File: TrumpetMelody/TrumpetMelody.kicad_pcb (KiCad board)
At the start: 2 copper layers, 76.2 x 68.6 mm, 81 parts, among them J1 USB_B_Micro, J2 Conn_01x05, J3 640456-3, J4 640456-3, SW1 SW_Push, U1 STM32F411RETx, U2 TLV62565DBVR, U3 MAX98357AETE_T, U4 MAX7375AXR805

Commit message: added alligator
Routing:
- net GND: vias 145 -> 146
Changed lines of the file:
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@@
   (via (at 165.735 83.058) (size 0.6604) (drill 0.381) (layers "F.Cu" "B.Cu") (free) (net 2))
   (via (at 203.105 102.37) (size 0.6604) (drill 0.381) (layers "F.Cu" "B.Cu") (free) (net 2))
+  (via (at 220.853 90.678) (size 1.8) (drill 0.9) (layers "F.Cu" "B.Cu") (net 2))
   (via (at 203.605 105.37) (size 0.6604) (drill 0.381) (layers "F.Cu" "B.Cu") (free) (net 2))
   (via (at 199.105 111.87) (size 0.6604) (drill 0.381) (layers "F.Cu" "B.Cu") (free) (net 2))

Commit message: cleaning
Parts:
- moved R25 1.53 mm to (197.6, 91.6)
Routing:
- net NJTRST: track 12.5 -> 13.6 mm
- net Net-(J2-Pin_5): track 2.96 -> 3.81 mm
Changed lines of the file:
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@@
   )
   (footprint "Resistor_SMD:R_0805_2012Metric_Pad1.20x1.40mm_HandSolder" (layer "F.Cu")
-    (at 196.287107 90.877107 -45)
+    (at 197.636622 91.606177 -45)
     (descr "Resistor SMD 0805 (2012 Metric), square (rectangular) end terminal, IPC_7351 nominal with elongated pad for handsoldering. (Body size source: IPC-SM-782 page 72, https://www.pcb-3d.com/wordpress/wp-content/uploads/ipc-sm-782a_amendment_1_and_2.pdf), generated with kicad-footprint-generator")
     (tags "resistor handsolder")
@@
   (segment (start 191.355 74.37) (end 191.355 75.681253) (width 0.254) (layer "B.Cu") (net 4))
   (segment (start 178.20837 66.87) (end 192.647803 66.87) (width 0.5) (layer "B.Cu") (net 4))
-  (segment (start 172.041482 67.375745) (end 172.054488 67.362739) (width 0.254) (layer "B.Cu") (net 4))
   (segment (start 170.545712 67.375745) (end 169.057454 67.375745) (width 0.5) (layer "B.Cu") (net 4))
   (segment (start 190.811123 79.038) (end 190.473126 79.038) (width 0.254) (layer "F.Cu") (net 5))
@@
   (via (at 205.105 88.62) (size 0.6604) (drill 0.381) (layers "F.Cu" "B.Cu") (free) (net 11))
   (segment (start 211.857768 68.152648) (end 211.857768 72.392265) (width 0.254) (layer "B.Cu") (net 11))
-  (segment (start 205.105 88.62) (end 195.605 88.62) (width 0.254) (layer "B.Cu") (net 11))
   (segment (start 211.84006 68.13494) (end 211.857768 68.152648) (width 0.254) (layer "B.Cu") (net 11))
-  (segment (start 192.903586 91.321414) (end 188.653585 91.321414) (width 0.254) (layer "B.Cu") (net 11))
-  (segment (start 195.605 88.62) (end 192.903586 91.321414) (width 0.254) (layer "B.Cu") (net 11))
+  (segment (start 196.6877 88.62) (end 193.986286 91.321414) (width 0.254) (layer "B.Cu") (net 11))
+  (segment (start 205.105 88.62) (end 196.6877 88.62) (width 0.254) (layer "B.Cu") (net 11))
+  (segment (start 193.986286 91.321414) (end 188.653585 91.321414) (width 0.254) (layer "B.Cu") (net 11))
   (segment (start 204.273075 58.783961) (end 203.233946 59.82309) (width 0.254) (layer "F.Cu") (net 12))
   (segment (start 203.168 55.9054) (end 206.6821 55.9054) (width 0.254) (layer "F.Cu") (net 12))
@@
   (via (at 211.060276 68.992484) (size 0.6604) (drill 0.381) (layers "F.Cu" "B.Cu") (free) (net 12))
   (segment (start 211.060276 68.992484) (end 211.060276 73.081437) (width 0.254) (layer "B.Cu") (net 12))
-  (segment (start 195.843974 87.62) (end 205.105 87.62) (width 0.254) (layer "B.Cu") (net 12))
+  (segment (start 193.996604 90.570706) (end 196.94731 87.62) (width 0.254) (layer "B.Cu") (net 12))
   (segment (start 211.060276 73.081437) (end 211.053703 73.08801) (width 0.254) (layer "B.Cu") (net 12))
-  (segment (start 189.225811 90.570706) (end 192.893268 90.570706) (width 0.254) (layer "B.Cu") (net 12))
-  (segment (start 192.893268 90.570706) (end 195.843974 87.62) (width 0.254) (layer "B.Cu") (net 12))
+  (segment (start 196.94731 87.62) (end 205.105 87.62) (width 0.254) (layer "B.Cu") (net 12))
+  (segment (start 189.225811 90.570706) (end 193.996604 90.570706) (width 0.254) (layer "B.Cu") (net 12))
   (segment (start 210.199926 68.627926) (end 209.651 68.079) (width 0.254) (layer "F.Cu") (net 13))
   (segment (start 189.235476 89.623544) (end 188.87017 89.623544) (width 0.254) (layer "F.Cu") (net 13))
@@
   (via (at 210.185 73.66) (size 0.6604) (drill 0.381) (layers "F.Cu" "B.Cu") (free) (net 13))
   (via (at 205.105 86.62) (size 0.6604) (drill 0.381) (layers "F.Cu" "B.Cu") (free) (net 13))
-  (segment (start 193.228 89.497) (end 193.101456 89.623544) (width 0.254) (layer "B.Cu") (net 13))
-  (segment (start 193.101456 89.623544) (end 189.235476 89.623544) (width 0.254) (layer "B.Cu") (net 13))
+  (segment (start 205.105 86.62) (end 197.188412 86.62) (width 0.254) (layer "B.Cu") (net 13))
   (segment (start 210.185 69.621241) (end 210.185 73.66) (width 0.254) (layer "B.Cu") (net 13))
-  (segment (start 205.105 86.62) (end 196.105 86.62) (width 0.254) (layer "B.Cu") (net 13))
-  (segment (start 196.105 86.62) (end 193.228 89.497) (width 0.254) (layer "B.Cu") (net 13))
+  (segment (start 197.188412 86.62) (end 194.184868 89.623544) (width 0.254) (layer "B.Cu") (net 13))
+  (segment (start 194.184868 89.623544) (end 189.235476 89.623544) (width 0.254) (layer "B.Cu") (net 13))
   (segment (start 210.199926 69.606315) (end 210.185 69.621241) (width 0.254) (layer "B.Cu") (net 13))
   (segment (start 174.133 57.783786) (end 174.316107 57.966893) (width 0.254) (layer "F.Cu") (net 14))
@@
   (segment (start 191.751308 93.98) (end 193.348154 95.576846) (width 0.254) (layer "F.Cu") (net 33))
   (segment (start 189.865 93.98) (end 191.751308 93.98) (width 0.254) (layer "F.Cu") (net 33))
-  (segment (start 195.144205 93.434223) (end 195.144205 93.780795) (width 0.254) (layer "F.Cu") (net 34))
-  (segment (start 196.994214 91.584214) (end 195.144205 93.434223) (width 0.254) (layer "F.Cu") (net 34))
+  (segment (start 198.343729 92.313284) (end 197.880986 92.313284) (width 0.254) (layer "F.Cu") (net 34))
+  (segment (start 196.413475 93.780795) (end 195.144205 93.780795) (width 0.254) (layer "F.Cu") (net 34))
+  (segment (start 197.880986 92.313284) (end 196.413475 93.780795) (width 0.254) (layer "F.Cu") (net 34))
   (segment (start 205.613 51.054) (end 209.546826 51.054) (width 0.254) (layer "F.Cu") (net 35))
   (segment (start 209.546826 51.054) (end 209.662118 50.938708) (width 0.254) (layer "F.Cu") (net 35))
@@
   (via (at 186.69 92.71) (size 0.6604) (drill 0.381) (layers "F.Cu" "B.Cu") (free) (net 48))
   (segment (start 186.69 92.71) (end 186.69 94.615) (width 0.254) (layer "B.Cu") (net 48))
-  (segment (start 195.58 90.17) (end 192.405 93.345) (width 0.254) (layer "F.Cu") (net 49))
-  (segment (start 192.405 93.345) (end 191.77 93.345) (width 0.254) (layer "F.Cu") (net 49))
+  (segment (start 195.149494 90.89907) (end 192.703564 93.345) (width 0.254) (layer "F.Cu") (net 49))
+  (segment (start 196.929515 90.89907) (end 195.149494 90.89907) (width 0.254) (layer "F.Cu") (net 49))
   (segment (start 191.77 93.345) (end 191.105 92.68) (width 0.254) (layer "F.Cu") (net 49))
+  (segment (start 192.703564 93.345) (end 191.77 93.345) (width 0.254) (layer "F.Cu") (net 49))
+  (segment (start 191.105 89.0272) (end 190.395146 89.0272) (width 0.254) (layer "F.Cu") (net 49))
+  (segment (start 191.105 92.68) (end 191.105 89.0272) (width 0.254) (layer "F.Cu") (net 49))
   (segment (start 190.395146 89.0272) (end 188.922037 87.554091) (width 0.254) (layer "F.Cu") (net 49))
-  (segment (start 191.105 92.68) (end 191.105 89.0272) (width 0.254) (layer "F.Cu") (net 49))
-  (segment (start 191.105 89.0272) (end 190.395146 89.0272) (width 0.254) (layer "F.Cu") (net 49))
   (segment (start 199.005 101.35) (end 199.005 103.34) (width 0.254) (layer "F.Cu") (net 50))
   (segment (start 200.66 99.695) (end 199.005 101.35) (width 0.254) (layer "F.Cu") (net 50))

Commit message: Finished PCB
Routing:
- net USB_ID_Connector: track 7.39 -> 6.58 mm
- net Net-(U3-SD_MODE): track 4.67 -> 4.10 mm

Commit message: Minor edits
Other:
- board text added: "ECE477 Team 15 Trumpet Melody CW CG SE KC - Rev. 1.1f"
- board text removed: "ECE477 Team 15 Trumpet Melody CW CG SE KC - Rev. 1.0"
- board text removed: "TBD: - is there a way to fully disregard the {dblquote}disconnected vias{dblquote} aka the stuff we decided to just throw out to a via for funsies? i moved to excluded violations but the arrows are still there and being annoying - organize planes to avoid interference for audio signals not sure if needed: - maybe a 3.3v power plane instead of traces on the top - i think we ignore moving 3.3V ics 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"
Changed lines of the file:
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@@
   (gr_rect locked (start 147.32 45.72) (end 223.52 114.3)
     (stroke (width 0.2) (type default)) (fill none) (layer "Edge.Cuts"))
-  (gr_text "TBD:\n- is there a way to fully disregard the {dblquote}disconnected vias{dblquote} aka the\nstuff we decided to just throw out to a via for funsies? i moved to \nexcluded violations but the arrows are still there and being annoying\n- organize planes to avoid interference for audio signals\n\nnot sure if needed:\n- maybe a 3.3v power plane instead of traces on the top \n- i think we ignore moving 3.3V ics to the front\n\ni also need someone else to look thru the whole schematic to verify \nno acute angles. i see none but someone wrote a comment about it so \neither i am blind or it was just general advice. pls help." (at 146.105 148.87) (layer "F.Cu")
-    (effects (font (size 1.5 1.5) (thickness 0.3) bold) (justify left bottom))
-  )
   (gr_text "TMS" (at 185.301178 98.92878 315) (layer "F.SilkS")
     (effects (font (size 1.016 0.635) (thickness 0.1524) bold) (justify left bottom))
@@
     (effects (font (size 1.016 0.635) (thickness 0.1524) bold) (justify left bottom))
   )
-  (gr_text "ECE477 Team 15 Trumpet Melody\nCW CG SE KC - Rev. 1.0" (at 158.355 113.62) (layer "F.SilkS")
+  (gr_text "ECE477 Team 15 Trumpet Melody\nCW CG SE KC - Rev. 1.1f" (at 158.355 113.62) (layer "F.SilkS")
     (effects (font (size 1.016 1) (thickness 0.1524)) (justify left bottom))
   )

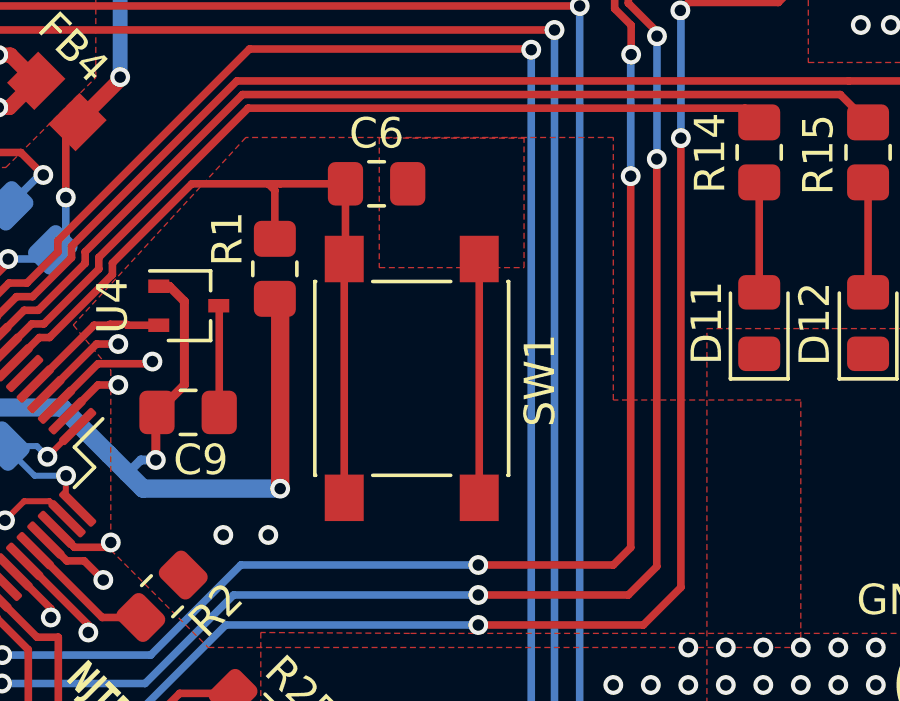
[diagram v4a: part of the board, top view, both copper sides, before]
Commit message: Changed button footprint and verified design
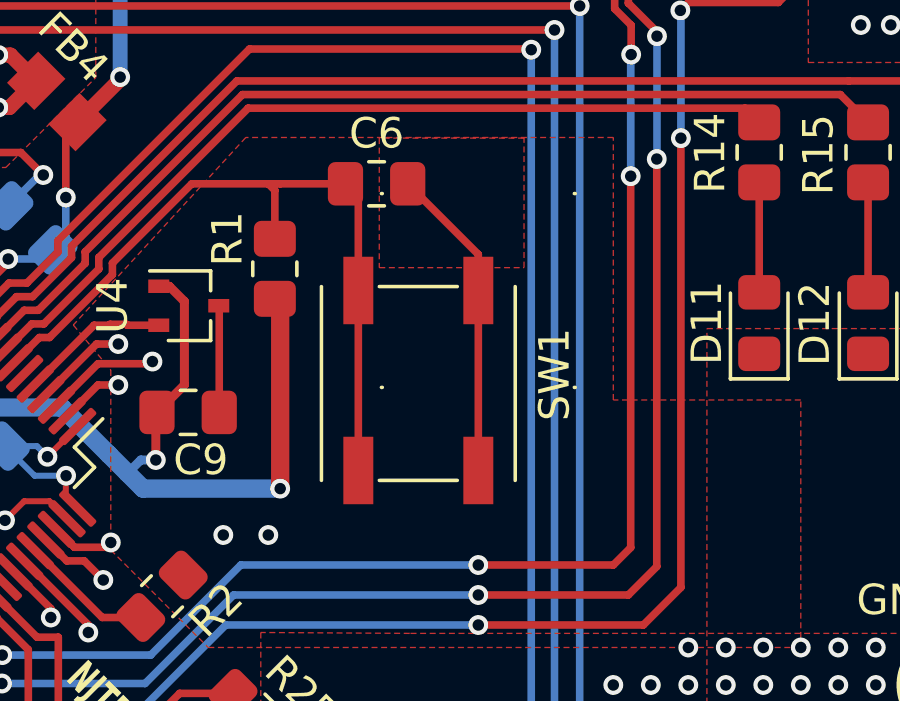
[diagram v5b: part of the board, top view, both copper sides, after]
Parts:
- moved SW1 3.68 mm to (205.1, 77.5)
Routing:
- net GND: track 52.0 -> 54.6 mm
- net NRST: track 26.2 -> 25.4 mm
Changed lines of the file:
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@@
   )
   (footprint "Button_Switch_SMD:SW_SPST_PTS645" (layer "F.Cu")
-    (at 202.885527 80.401051 -90)
+    (at 205.105 77.47 -90)
     (descr "C&K Components SPST SMD PTS645 Series 6mm Tact Switch")
     (tags "SPST Button Switch")
@@
     (property "ki_keywords" "switch normally-open pushbutton push-button")
     (attr smd)
-    (fp_text reference "SW1" (at 0.066923 -4.276905 90) (layer "F.SilkS")
-        (effects (font (size 1.016 1) (thickness 0.1524)))
-    )
-    (fp_text value "SW_Push" (at 0 4.15 90) (layer "F.Fab")
-        (effects (font (size 1 1) (thickness 0.15)))
-    )
-    (fp_text user "${REFERENCE}" (at 0 -4.05 90) (layer "F.Fab")
-        (effects (font (size 1 1) (thickness 0.15)))
-    )
-    (fp_line (start -3.23 -3.23) (end 3.23 -3.23)
-      (stroke (width 0.12) (type solid)) (layer "F.SilkS"))
+    (fp_text reference "SW1" (at 2.8 -2.54 90) (layer "F.SilkS")
+        (effects (font (size 1.016 1) (thickness 0.1524)))
+    )
+    (fp_text value "SW_Push" (at 3.1 6.2 90) (layer "F.Fab")
+        (effects (font (size 1 1) (thickness 0.15)))
+    )
+    (fp_text user "${REFERENCE}" (at 3 -3.4 90) (layer "F.Fab")
+        (effects (font (size 1 1) (thickness 0.15)))
+    )
     (fp_line (start -3.23 -3.2) (end -3.23 -3.23)
       (stroke (width 0.12) (type solid)) (layer "F.SilkS"))
-    (fp_line (start -3.23 -1.3) (end -3.23 1.3)
-      (stroke (width 0.12) (type solid)) (layer "F.SilkS"))
     (fp_line (start -3.23 3.23) (end -3.23 3.2)
       (stroke (width 0.12) (type solid)) (layer "F.SilkS"))
-    (fp_line (start -3.23 3.23) (end 3.23 3.23)
+    (fp_line (start -0.13 -1.23) (end 6.33 -1.23)
+      (stroke (width 0.12) (type solid)) (layer "F.SilkS"))
+    (fp_line (start -0.13 0.7) (end -0.13 3.3)
+      (stroke (width 0.12) (type solid)) (layer "F.SilkS"))
+    (fp_line (start -0.13 5.23) (end 6.33 5.23)
       (stroke (width 0.12) (type solid)) (layer "F.SilkS"))
     (fp_line (start 3.23 -3.23) (end 3.23 -3.2)
       (stroke (width 0.12) (type solid)) (layer "F.SilkS"))
-    (fp_line (start 3.23 -1.3) (end 3.23 1.3)
-      (stroke (width 0.12) (type solid)) (layer "F.SilkS"))
     (fp_line (start 3.23 3.23) (end 3.23 3.2)
       (stroke (width 0.12) (type solid)) (layer "F.SilkS"))
-    (fp_line (start -5.05 -3.4) (end -5.05 3.4)
-      (stroke (width 0.05) (type solid)) (layer "F.CrtYd"))
-    (fp_line (start -5.05 -3.4) (end 5.05 -3.4)
-      (stroke (width 0.05) (type solid)) (layer "F.CrtYd"))
-    (fp_line (start -5.05 3.4) (end 5.05 3.4)
-      (stroke (width 0.05) (type solid)) (layer "F.CrtYd"))
-    (fp_line (start 5.05 3.4) (end 5.05 -3.4)
-      (stroke (width 0.05) (type solid)) (layer "F.CrtYd"))
-    (fp_line (start -3 -3) (end -3 3)
-      (stroke (width 0.1) (type solid)) (layer "F.Fab"))
-    (fp_line (start -3 3) (end 3 3)
-      (stroke (width 0.1) (type solid)) (layer "F.Fab"))
-    (fp_line (start 3 -3) (end -3 -3)
-      (stroke (width 0.1) (type solid)) (layer "F.Fab"))
-    (fp_line (start 3 3) (end 3 -3)
-      (stroke (width 0.1) (type solid)) (layer "F.Fab"))
-    (fp_circle (center 0 0) (end 1.75 -0.05)
+    (fp_line (start 6.33 0.7) (end 6.33 3.3)
+      (stroke (width 0.12) (type solid)) (layer "F.SilkS"))
+    (fp_line (start -1.95 -1.4) (end -1.95 5.4)
+      (stroke (width 0.05) (type solid)) (layer "F.CrtYd"))
+    (fp_line (start -1.95 -1.4) (end 8.15 -1.4)
+      (stroke (width 0.05) (type solid)) (layer "F.CrtYd"))
+    (fp_line (start -1.95 5.4) (end 8.15 5.4)
+      (stroke (width 0.05) (type solid)) (layer "F.CrtYd"))
+    (fp_line (start 8.15 5.4) (end 8.15 -1.4)
+      (stroke (width 0.05) (type solid)) (layer "F.CrtYd"))
+    (fp_line (start 0.1 -1) (end 0.1 5)
+      (stroke (width 0.1) (type solid)) (layer "F.Fab"))
+    (fp_line (start 0.1 5) (end 6.1 5)
+      (stroke (width 0.1) (type solid)) (layer "F.Fab"))
+    (fp_line (start 6.1 -1) (end 0.1 -1)
+      (stroke (width 0.1) (type solid)) (layer "F.Fab"))
+    (fp_line (start 6.1 5) (end 6.1 -1)
+      (stroke (width 0.1) (type solid)) (layer "F.Fab"))
+    (fp_circle (center 3.1 2) (end 4.85 1.95)
       (stroke (width 0.1) (type solid)) (fill none) (layer "F.Fab"))
-    (pad "1" smd rect (at -3.98 -2.25 270) (size 1.55 1.3) (layers "F.Cu" "F.Paste" "F.Mask")
+    (pad "1" smd rect (at 0 0 270) (size 2.25 1) (layers "F.Cu" "F.Paste" "F.Mask")
       (net 2 "GND") (pinfunction "1") (pintype "passive"))
-    (pad "1" smd rect (at 3.98 -2.25 270) (size 1.55 1.3) (layers "F.Cu" "F.Paste" "F.Mask")
+    (pad "1" smd rect (at 6 0 270) (size 2.25 1) (layers "F.Cu" "F.Paste" "F.Mask")
       (net 2 "GND") (pinfunction "1") (pintype "passive"))
-    (pad "2" smd rect (at -3.98 2.25 270) (size 1.55 1.3) (layers "F.Cu" "F.Paste" "F.Mask")
+    (pad "2" smd rect (at 0 4 270) (size 2.25 1) (layers "F.Cu" "F.Paste" "F.Mask")
       (net 5 "NRST") (pinfunction "2") (pintype "passive"))
-    (pad "2" smd rect (at 3.98 2.25 270) (size 1.55 1.3) (layers "F.Cu" "F.Paste" "F.Mask")
+    (pad "2" smd rect (at 6 4 270) (size 2.25 1) (layers "F.Cu" "F.Paste" "F.Mask")
       (net 5 "NRST") (pinfunction "2") (pintype "passive"))
     (model "${KICAD6_3DMODEL_DIR}/Button_Switch_SMD.3dshapes/SW_SPST_PTS645.wrl"
@@
   (segment (start 190.36857 70.48057) (end 189.508 69.62) (width 0.5) (layer "F.Cu") (net 2))
   (segment (start 198.505 101.733286) (end 198.245857 101.474143) (width 0.254) (layer "F.Cu") (net 2))
-  (segment (start 205.135527 76.421051) (end 205.135527 84.381051) (width 0.254) (layer "F.Cu") (net 2))
   (segment (start 184.105 85.37) (end 185.855 83.62) (width 0.254) (layer "F.Cu") (net 2))
   (segment (start 189.47914 71.37) (end 189.105 71.37) (width 0.5) (layer "F.Cu") (net 2))
@@
   (segment (start 181.2544 73.7108) (end 180.5432 74.422) (width 0.254) (layer "F.Cu") (net 2))
   (segment (start 183.371249 77.053555) (end 184.2021 77.884406) (width 0.2) (layer "F.Cu") (net 2))
+  (segment (start 205.105 77.47) (end 205.105 76.266989) (width 0.254) (layer "F.Cu") (net 2))
   (segment (start 196.469 77.994) (end 196.453 77.978) (width 0.254) (layer "F.Cu") (net 2))
   (segment (start 178.775055 81.649749) (end 179.34598 82.220675) (width 0.2) (layer "F.Cu") (net 2))
@@
   (segment (start 191.396911 85.079217) (end 190.812508 84.494814) (width 0.2) (layer "F.Cu") (net 2))
   (segment (start 196.469 81.534) (end 196.469 77.994) (width 0.254) (layer "F.Cu") (net 2))
+  (segment (start 205.105 77.47) (end 205.105 83.47) (width 0.254) (layer "F.Cu") (net 2))
   (segment (start 184.2021 77.884406) (end 184.555653 77.884406) (width 0.2) (layer "F.Cu") (net 2))
   (segment (start 201.575999 104.525) (end 200.19 104.525) (width 0.254) (layer "F.Cu") (net 2))
@@
   (segment (start 180.489789 81.95027) (end 181.196896 81.243163) (width 0.2) (layer "F.Cu") (net 2))
   (segment (start 190.812508 84.494814) (end 189.96606 84.494814) (width 0.2) (layer "F.Cu") (net 2))
+  (segment (start 205.105 76.266989) (end 202.752011 73.914) (width 0.254) (layer "F.Cu") (net 2))
   (segment (start 189.508 69.62) (end 189.105 69.62) (width 0.5) (layer "F.Cu") (net 2))
   (segment (start 185.085983 88.667784) (end 185.616313 88.137454) (width 0.2) (layer "F.Cu") (net 2))
@@
   (segment (start 190.811123 79.038) (end 190.473126 79.038) (width 0.254) (layer "F.Cu") (net 5))
   (segment (start 190.473126 79.038) (end 189.629144 79.881982) (width 0.254) (layer "F.Cu") (net 5))
+  (segment (start 200.677011 73.914) (end 201.105 74.341989) (width 0.254) (layer "F.Cu") (net 5))
   (segment (start 195.553156 73.914) (end 192.908614 76.558542) (width 0.254) (layer "F.Cu") (net 5))
-  (segment (start 200.635527 76.421051) (end 200.635527 84.381051) (width 0.254) (layer "F.Cu") (net 5))
   (segment (start 192.908614 76.558542) (end 192.908615 76.940507) (width 0.254) (layer "F.Cu") (net 5))
   (segment (start 198.501 73.914) (end 198.105 73.914) (width 0.254) (layer "F.Cu") (net 5))
   (segment (start 198.105 73.914) (end 195.553156 73.914) (width 0.254) (layer "F.Cu") (net 5))
   (segment (start 198.32297 75.747943) (end 198.32297 74.13197) (width 0.254) (layer "F.Cu") (net 5))
+  (segment (start 201.105 74.341989) (end 201.105 77.47) (width 0.254) (layer "F.Cu") (net 5))
   (segment (start 198.32297 74.13197) (end 198.105 73.914) (width 0.254) (layer "F.Cu") (net 5))
   (segment (start 200.677011 73.914) (end 198.501 73.914) (width 0.254) (layer "F.Cu") (net 5))
   (segment (start 192.908615 76.940507) (end 190.811123 79.038) (width 0.254) (layer "F.Cu") (net 5))
-  (segment (start 200.677011 73.914) (end 200.677011 76.379567) (width 0.254) (layer "F.Cu") (net 5))
-  (segment (start 200.677011 76.379567) (end 200.635527 76.421051) (width 0.254) (layer "F.Cu") (net 5))
+  (segment (start 201.105 77.47) (end 201.105 83.47) (width 0.254) (layer "F.Cu") (net 5))
   (segment (start 192.065 105.41) (end 193.105 104.37) (width 0.61) (layer "F.Cu") (net 6))
   (segment (start 154.278422 97.872954) (end 153.280224 96.874756) (width 0.61) (layer "F.Cu") (net 6))
